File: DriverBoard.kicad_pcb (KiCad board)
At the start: 2 copper layers, 80 x 60 mm, 90 parts, among them J1 Conn_02x07_Odd_Even, J2 Conn_02x07_Odd_Even, Q1 HYG025N06LS1C2, Q2 HYG025N06LS1C2, Q3 HYG025N06LS1C2, Q4 HYG025N06LS1C2, Q5 HYG025N06LS1C2, Q6 HYG025N06LS1C2, U2 SCT2610, U4 SCT2420, U5 XT30PW-M

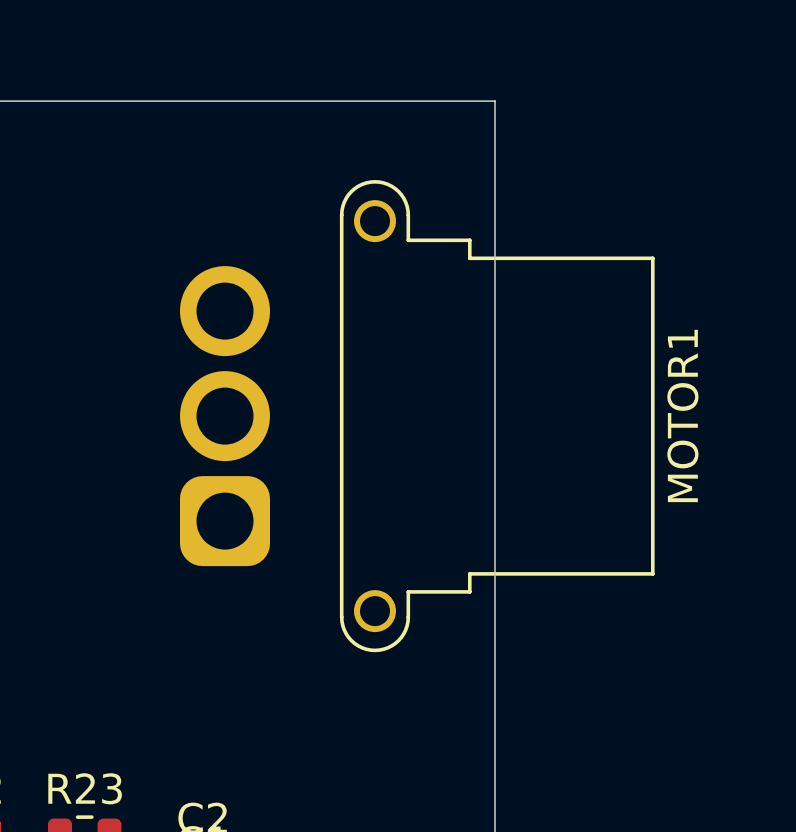
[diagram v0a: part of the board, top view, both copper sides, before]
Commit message: 工程增加环境变量
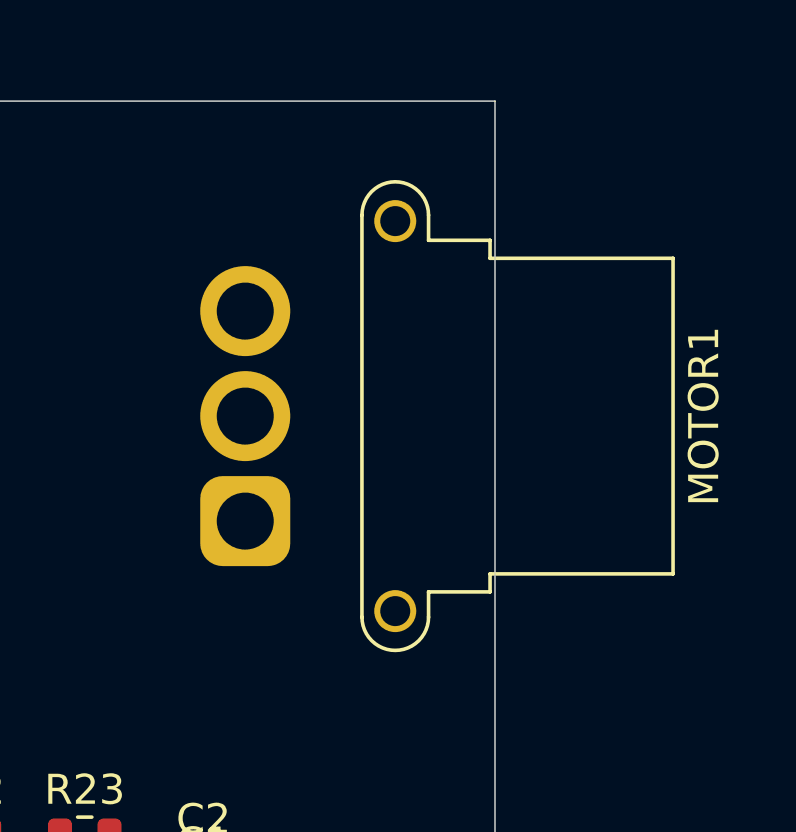
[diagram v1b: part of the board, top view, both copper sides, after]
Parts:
- moved MOTOR1 0.68 mm to (188.7, 63.0)

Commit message: 增加DXF文件夹
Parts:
- moved J1 42.0 mm to (122.0, 61.0)
- moved J2 36.1 mm to (123.5, 92.5)
- moved Q2 16.3 mm to (180.9, 63.9)
- moved Q1 15.4 mm to (172.9, 69.7)
- moved Q4 14.0 mm to (181.0, 57.9)
- moved Q6 13.5 mm to (180.5, 69.7)
- moved D1 11.2 mm to (153.0, 85.0), turned to 180 degrees
- moved Q5 8.53 mm to (173.7, 58.4)
- moved MOTOR1 4.55 mm to (188.0, 67.5)
- moved Q3 4.01 mm to (173.0, 64.2)
- moved U5 1.19 mm to (124.7, 81.5)
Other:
- outline, holes or cut-outs redrawn
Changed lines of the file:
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@@
 	(footprint "footprints:XT30PW-F_1x02_P2.50mm_Horizontal"
 		(layer "F.Cu")
-		(at 125.15 80.425 90)
+		(at 124.65 81.5 90)
 		(descr "Connector XT30 Horizontal PCB Female, https://www.tme.eu/Document/f383737e340bfdab1f665284174b4ea2/XT30PW-F.pdf")
 		(tags "RC Connector XT30")
@@
 	(footprint "Diode_SMD:D_SMB"
 		(layer "F.Cu")
-		(at 163.675 81.61)
+		(at 153 85 180)
 		(descr "Diode SMB (DO-214AA)")
 		(tags "Diode SMB (DO-214AA)")
@@
 		)
 		(property "Datasheet" ""
-			(at 0 0 0)
+			(at 0 0 180)
 			(unlocked yes)
 			(layer "F.Fab")
@@
 		)
 		(property "Description" ""
-			(at 0 0 0)
+			(at 0 0 180)
 			(unlocked yes)
 			(layer "F.Fab")
@@
 		(attr smd)
 		(fp_line
-			(start -3.66 -2.15)
-			(end -3.66 2.15)
+			(start -3.66 2.15)
+			(end 2.15 2.15)
 			(stroke
 				(width 0.12)
@@
 		)
 		(fp_line
-			(start -3.66 2.15)
-			(end 2.15 2.15)
+			(start -3.66 -2.15)
+			(end -3.66 2.15)
 			(stroke
 				(width 0.12)
@@
 		)
 		(fp_line
-			(start -3.65 -2.25)
-			(end 3.65 -2.25)
+			(start 3.65 2.25)
+			(end -3.65 2.25)
 			(stroke
 				(width 0.05)
@@
 		)
 		(fp_line
-			(start -3.65 2.25)
-			(end -3.65 -2.25)
+			(start 3.65 -2.25)
+			(end 3.65 2.25)
 			(stroke
 				(width 0.05)
@@
 		)
 		(fp_line
-			(start 3.65 -2.25)
-			(end 3.65 2.25)
+			(start -3.65 2.25)
+			(end -3.65 -2.25)
 			(stroke
 				(width 0.05)
@@
 		)
 		(fp_line
-			(start 3.65 2.25)
-			(end -3.65 2.25)
+			(start -3.65 -2.25)
+			(end 3.65 -2.25)
 			(stroke
 				(width 0.05)
@@
 		)
 		(fp_line
-			(start -2.3 2)
-			(end -2.3 -2)
+			(start 2.3 2)
+			(end -2.3 2)
 			(stroke
 				(width 0.1)
@@
 		)
 		(fp_line
-			(start -0.64944 -0.79908)
-			(end -0.64944 0.80112)
+			(start 2.3 -2)
+			(end 2.3 2)
 			(stroke
 				(width 0.1)
@@
 		)
 		(fp_line
-			(start -0.64944 0.00102)
-			(end -1.55114 0.00102)
+			(start 2.3 -2)
+			(end -2.3 -2)
 			(stroke
 				(width 0.1)
@@
 		)
 		(fp_line
-			(start -0.64944 0.00102)
+			(start 0.50118 0.75032)
 			(end 0.50118 -0.79908)
 			(stroke
@@
 		)
 		(fp_line
-			(start -0.64944 0.00102)
-			(end 0.50118 0.75032)
+			(start 0.50118 0.00102)
+			(end 1.4994 0.00102)
 			(stroke
 				(width 0.1)
@@
 		)
 		(fp_line
-			(start 0.50118 0.00102)
-			(end 1.4994 0.00102)
+			(start -0.64944 0.00102)
+			(end 0.50118 0.75032)
 			(stroke
 				(width 0.1)
@@
 		)
 		(fp_line
-			(start 0.50118 0.75032)
+			(start -0.64944 0.00102)
 			(end 0.50118 -0.79908)
 			(stroke
@@
 		)
 		(fp_line
-			(start 2.3 -2)
-			(end -2.3 -2)
+			(start -0.64944 0.00102)
+			(end -1.55114 0.00102)
 			(stroke
 				(width 0.1)
@@
 		)
 		(fp_line
-			(start 2.3 -2)
-			(end 2.3 2)
+			(start -0.64944 -0.79908)
+			(end -0.64944 0.80112)
 			(stroke
 				(width 0.1)
@@
 		)
 		(fp_line
-			(start 2.3 2)
-			(end -2.3 2)
+			(start -2.3 2)
+			(end -2.3 -2)
 			(stroke
 				(width 0.1)
@@
 		)
 		(pad "1" smd roundrect
-			(at -2.15 0)
+			(at -2.15 0 180)
 			(size 2.5 2.3)
 			(layers "F.Cu" "F.Mask" "F.Paste")
@@
 		)
 		(pad "2" smd roundrect
-			(at 2.15 0)
+			(at 2.15 0 180)
 			(size 2.5 2.3)
 			(layers "F.Cu" "F.Mask" "F.Paste")
@@
 	(footprint "footprints:HYG025N06LS1C2-PDFN-8-1EP_6x5mm_P1.27mm_EP3x3mm"
 		(layer "F.Cu")
-		(at 175.275 60.9)
+		(at 173.045 64.23)
 		(descr "W-PDFN, 8 Pin (https://media-www.micron.com/-/media/client/global/documents/products/data-sheet/nor-flash/serial-nor/mt25q/die-rev-a/mt25q_qljs_u_256_aba_0.pdf#page=22), generated with kicad-footprint-generator ipc_noLead_generator.py")
 		(tags "W-PDFN NoLead")
@@
 	(footprint "footprints:MR30PW-FB_1x03_P3.50mm_Horizontal"
 		(layer "F.Cu")
-		(at 188.675 63 -90)
+		(at 188 67.5 -90)
 		(descr "Connector MR30 Horizontal PCB Female, https://www.tme.eu/Document/4a6895c4a2c7eddf355b391fd904cb53/MR30PW-FB.pdf")
 		(tags "RC Connector MR30")
@@
 	(footprint "footprints:HYG025N06LS1C2-PDFN-8-1EP_6x5mm_P1.27mm_EP3x3mm"
 		(layer "F.Cu")
-		(at 167.35 66.75)
+		(at 180.51 69.71)
 		(descr "W-PDFN, 8 Pin (https://media-www.micron.com/-/media/client/global/documents/products/data-sheet/nor-flash/serial-nor/mt25q/die-rev-a/mt25q_qljs_u_256_aba_0.pdf#page=22), generated with kicad-footprint-generator ipc_noLead_generator.py")
 		(tags "W-PDFN NoLead")
@@
 	(footprint "footprints:HYG025N06LS1C2-PDFN-8-1EP_6x5mm_P1.27mm_EP3x3mm"
 		(layer "F.Cu")
-		(at 175.75 66.635)
+		(at 173.65 58.365)
 		(descr "W-PDFN, 8 Pin (https://media-www.micron.com/-/media/client/global/documents/products/data-sheet/nor-flash/serial-nor/mt25q/die-rev-a/mt25q_qljs_u_256_aba_0.pdf#page=22), generated with kicad-footprint-generator ipc_noLead_generator.py")
 		(tags "W-PDFN NoLead")
@@
 	(footprint "footprints:HYG025N06LS1C2-PDFN-8-1EP_6x5mm_P1.27mm_EP3x3mm"
 		(layer "F.Cu")
-		(at 167.925 53.98)
+		(at 180.91 63.865)
 		(descr "W-PDFN, 8 Pin (https://media-www.micron.com/-/media/client/global/documents/products/data-sheet/nor-flash/serial-nor/mt25q/die-rev-a/mt25q_qljs_u_256_aba_0.pdf#page=22), generated with kicad-footprint-generator ipc_noLead_generator.py")
 		(tags "W-PDFN NoLead")
@@
 	(footprint "footprints:HYG025N06LS1C2-PDFN-8-1EP_6x5mm_P1.27mm_EP3x3mm"
 		(layer "F.Cu")
-		(at 175.35 54.48)
+		(at 172.87 69.71)
 		(descr "W-PDFN, 8 Pin (https://media-www.micron.com/-/media/client/global/documents/products/data-sheet/nor-flash/serial-nor/mt25q/die-rev-a/mt25q_qljs_u_256_aba_0.pdf#page=22), generated with kicad-footprint-generator ipc_noLead_generator.py")
 		(tags "W-PDFN NoLead")
@@
 	(footprint "Connector_PinSocket_1.27mm:PinSocket_2x07_P1.27mm_Vertical_SMD"
 		(layer "F.Cu")
-		(at 121.8 103)
+		(at 122 61)
 		(descr "surface-mounted straight socket strip, 2x07, 1.27mm pitch, double cols (from Kicad 4.0.7!), script generated")
 		(tags "Surface mounted socket strip SMD 2x07 1.27mm double row")
@@
 	(footprint "footprints:HYG025N06LS1C2-PDFN-8-1EP_6x5mm_P1.27mm_EP3x3mm"
 		(layer "F.Cu")
-		(at 167.35 60.75)
+		(at 181.01 57.865)
 		(descr "W-PDFN, 8 Pin (https://media-www.micron.com/-/media/client/global/documents/products/data-sheet/nor-flash/serial-nor/mt25q/die-rev-a/mt25q_qljs_u_256_aba_0.pdf#page=22), generated with kicad-footprint-generator ipc_noLead_generator.py")
 		(tags "W-PDFN NoLead")
@@
 	(footprint "Connector_PinSocket_1.27mm:PinSocket_2x07_P1.27mm_Vertical_SMD"
 		(layer "F.Cu")
-		(at 121.8 56.46)
+		(at 123.5 92.5)
 		(descr "surface-mounted straight socket strip, 2x07, 1.27mm pitch, double cols (from Kicad 4.0.7!), script generated")
 		(tags "Surface mounted socket strip SMD 2x07 1.27mm double row")
@@
 		)
 	)
-	(gr_line
-		(start 117 78)
-		(end 197 78)
+	(gr_circle
+		(center 121 53.5)
+		(end 122.6 53.5)
+		(stroke
+			(width 0.5)
+			(type default)
+		)
+		(fill no)
+		(layer "Dwgs.User")
+	)
+	(gr_circle
+		(center 121 103.5)
+		(end 122.6 103.5)
+		(stroke
+			(width 0.5)
+			(type default)
+		)
+		(fill no)
+		(layer "Dwgs.User")
+	)
+	(gr_arc
+		(start 122 108.5)
+		(mid 117.757359 106.742641)
+		(end 116 102.5)
+		(stroke
+			(width 0.5)
+			(type solid)
+		)
+		(layer "Edge.Cuts")
+	)
+	(gr_arc
+		(start 190 48.5)
+		(mid 194.242641 50.257359)
+		(end 196 54.5)
 		(stroke
-			(width 0.1)
+			(width 0.5)
 			(type solid)
 		)
-		(layer "F.SilkS")
+		(layer "Edge.Cuts")
+	)
+	(gr_arc
+		(start 116 54.5)
+		(mid 117.757359 50.257359)
+		(end 122 48.5)
+		(stroke
+			(width 0.5)
+			(type solid)
+		)
+		(layer "Edge.Cuts")
 	)
 	(gr_line
-		(start 117 49)
-		(end 197 49)
+		(start 116 54.5)
+		(end 116 102.5)
 		(stroke
-			(width 0.05)
-			(type default)
+			(width 0.5)
+			(type solid)
+		)
+		(layer "Edge.Cuts")
+	)
+	(gr_circle
+		(center 191 103.5)
+		(end 192.6 103.5)
+		(stroke
+			(width 0.5)
+			(type solid)
 		)
+		(fill no)
 		(layer "Edge.Cuts")
 	)
 	(gr_line
-		(start 197 109)
-		(end 117 109)
+		(start 190 48.5)
+		(end 122 48.5)
 		(stroke
-			(width 0.05)
-			(type default)
+			(width 0.5)
+			(type solid)
+		)
+		(layer "Edge.Cuts")
+	)
+	(gr_arc
+		(start 196 102.5)
+		(mid 194.242641 106.742641)
+		(end 190 108.5)
+		(stroke
+			(width 0.5)
+			(type solid)
 		)
 		(layer "Edge.Cuts")
 	)
 	(gr_line
-		(start 197 49)
-		(end 197 109)
+		(start 196 102.5)
+		(end 196 54.5)
 		(stroke
-			(width 0.05)
-			(type default)
+			(width 0.5)
+			(type solid)
+		)
+		(layer "Edge.Cuts")
+	)
+	(gr_circle
+		(center 191 53.5)
+		(end 192.6 53.5)
+		(stroke
+			(width 0.5)
+			(type solid)
 		)
+		(fill no)
 		(layer "Edge.Cuts")
 	)
 	(gr_line
-		(start 117 109)
-		(end 117 49)
+		(start 122 108.5)
+		(end 190 108.5)
 		(stroke
-			(width 0.05)
-			(type default)
+			(width 0.5)
+			(type solid)
 		)
 		(layer "Edge.Cuts")
 	)
+	(gr_line
+		(start 116 78.5)
+		(end 196 78.5)
+		(stroke
+			(width 0.5)
+			(type solid)
+		)
+		(layer "User.1")
+	)
 	(embedded_fonts no)

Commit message: 三相桥基极增加回流路径,增加VDC的输入电容
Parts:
- removed U5: XT30PW-M, footprints:XT30PW-F_1x02_P2.50mm_Horizontal
- added C30: 4.7uF, Capacitor_SMD:C_1206_3216Metric, F.Cu at (176.5, 90.0)
- added C31: 4.7uF, Capacitor_SMD:C_1206_3216Metric, F.Cu at (176.5, 93.0)
- added C35: 4.7uF, Capacitor_SMD:C_1206_3216Metric, F.Cu at (176.5, 96.0)
- added C36: 4.7uF, Capacitor_SMD:C_1206_3216Metric, F.Cu at (176.5, 99.0)
- added C37: 4.7uF, Capacitor_SMD:C_1206_3216Metric, F.Cu at (176.5, 102.0)
- added C38: 4.7uF, Capacitor_SMD:C_1206_3216Metric, F.Cu at (176.5, 105.0)
- added D10: SODF107-SH, Diode_SMD:D_SOD-123F, F.Cu at (162.4, 103.0)
- added D4: SODF107-SH, Diode_SMD:D_SOD-123F, F.Cu at (162.3, 89.0)
- added D5: SODF107-SH, Diode_SMD:D_SOD-123F, F.Cu at (162.4, 91.3)
- added D6: SODF107-SH, Diode_SMD:D_SOD-123F, F.Cu at (162.4, 94.0)
- added D8: SODF107-SH, Diode_SMD:D_SOD-123F, F.Cu at (162.4, 97.0)
- added D9: SODF107-SH, Diode_SMD:D_SOD-123F, F.Cu at (162.4, 100.0)
- added U6: ~, footprints:XT30PW-F_1x02_P2.50mm_Horizontal, F.Cu at (122.0, 80.0)
- D2, D3, D7: value SS1P3L-M3 -> SODF107-SH; footprint Diode_SMD:D_SMP_DO-220AA -> Diode_SMD:D_SOD-123F
- moved D2 47.0 mm to (167.3, 90.0)
- moved D3 46.3 mm to (167.3, 93.3)
- moved D7 45.6 mm to (167.3, 96.7)

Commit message: 优化原理图
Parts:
- added C27: 0.1uF/100V, Capacitor_SMD:C_0603_1608Metric, F.Cu at (169.0, 78.5)
- added C8: 2.2uF, Capacitor_SMD:C_0603_1608Metric, F.Cu at (133.2, 74.0)
- moved C28 44.2 mm to (181.4, 52.0), turned to 90 degrees
- moved C25 41.0 mm to (179.2, 52.0), turned to 90 degrees
- moved C23 38.0 mm to (177.0, 52.0), turned to 90 degrees
- moved R28 26.8 mm to (161.2, 65.3), turned to 90 degrees
- moved R22 26.2 mm to (136.5, 61.0)
- moved R29 25.1 mm to (159.6, 65.3), turned to 90 degrees
- moved R18 22.6 mm to (129.3, 66.0)
- moved C20 22.6 mm to (134.0, 63.4)
- moved C21 22.6 mm to (134.0, 65.9)
- moved R16 22.6 mm to (129.3, 63.5)
- moved R19 22.6 mm to (129.3, 68.5)
- moved R21 19.3 mm to (131.5, 51.0)
- moved R30 17.9 mm to (155.0, 68.4)
- moved R37 17.4 mm to (161.5, 61.8), turned to 90 degrees
- moved R35 17.0 mm to (158.0, 61.8), turned to 90 degrees
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- renumbered C10 to C1, C4 to C10, C13 to C11, C5 to C12, C15 to C13, C16 to C14, C17 to C15, C8 to C16, C6 to C17, C7 to C18, C26 to C19, C11 to C2, C27 to C20, C28 to C21, C29 to C22, C30 to C23, C36 to C24, C31 to C25, C37 to C26, C35 to C28, C38 to C29, C12 to C3, C20 to C30, C23 to C31, C9 to C32, C19 to C33, C33 to C34, C32 to C35, C34 to C36, C21 to C37, C22 to C38, C24 to C39, C18 to C4, C25 to C40, C1 to C5, C2 to C6, C3 to C7, C14 to C9, D3 to D10, D4 to D2, D5 to D3, D6 to D4, D8 to D5, D10 to D6, D9 to D7, D7 to D8, D2 to D9, L2 to L1, L1 to L2, Q6 to Q1, Q1 to Q2, Q2 to Q3, Q3 to Q4, Q4 to Q5, Q5 to Q6, R18 to R1, R22 to R10, R12 to R11, R13 to R12, R1 to R13, R2 to R14, R24 to R15, R25 to R16, R15 to R17, R26 to R18, R27 to R19, R19 to R2, R3 to R20, R28 to R21, R29 to R22, R4 to R23, R40 to R24, R43 to R25, R38 to R26, R39 to R27, R41 to R28, R42 to R29, R20 to R3, R44 to R30, R30 to R31, R31 to R32, R32 to R33, R33 to R34, R34 to R35, R35 to R36, R36 to R37, R37 to R38, R9 to R4, R10 to R5, R11 to R6, R23 to R7, R14 to R8, R21 to R9, U6 to U1, U4 to U2, U2 to U3, U1 to U4, U3 to U5
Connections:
- C23 pad 2: GND -> GNDPWR
- C24 pad 2: GND -> GNDPWR
- C25 pad 2: GND -> GNDPWR
- C26 pad 2: GND -> GNDPWR
- C28 pad 2: GND -> GNDPWR
- C29 pad 2: GND -> GNDPWR
- R17 pad 2: GND -> GNDPWR
- R20 pad 2: GND -> GNDPWR
- R23 pad 2: GND -> GNDPWR

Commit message: 修改板框文件
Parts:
- moved U1 60.1 mm to (182.4, 73.7), turned to -90 degrees
- moved D8 59.1 mm to (128.2, 52.4), turned to 180 degrees
- moved D10 53.2 mm to (128.2, 57.3), turned to 180 degrees
- moved D9 52.6 mm to (128.2, 54.8), turned to 180 degrees
- moved R7 52.3 mm to (131.1, 72.9)
- moved C4 51.5 mm to (123.9, 78.4)
- moved C15 48.6 mm to (127.2, 79.9)
- moved R16 46.9 mm to (175.4, 72.3)
- moved L1 46.5 mm to (140.2, 73.7), turned to 180 degrees
- moved C16 45.2 mm to (173.0, 82.5)
- moved R18 42.7 mm to (172.1, 65.6), turned to -90 degrees
- moved R15 40.5 mm to (180.0, 65.6), turned to 90 degrees
- moved C8 40.1 mm to (172.7, 81.0)
- moved D6 39.5 mm to (164.3, 61.6), turned to 90 degrees
- moved C20 39.0 mm to (172.5, 57.2), turned to -90 degrees
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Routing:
- net /Pre_Driver/W1: track 0.00 -> 33.8 mm, vias 0 -> 1
- net /Pre_Driver/V1: track 0.00 -> 23.0 mm, vias 0 -> 1
- net /Pre_Driver/U1: track 0.00 -> 10.8 mm, vias 0 -> 1
- net /ThreePhase/U1_CURR: track 0.00 -> 4.98 mm
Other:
- outline, holes or cut-outs redrawn

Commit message: 优化电源布局,优化中
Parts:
- moved R12 37.8 mm to (143.6, 93.7)
- moved R11 34.6 mm to (141.9, 93.7)
- moved R17 31.3 mm to (179.0, 36.6)
- moved R20 31.3 mm to (171.0, 36.6)
- moved R22 31.3 mm to (161.9, 41.0)
- moved R23 31.3 mm to (162.9, 36.6)
- moved C21 31.3 mm to (166.7, 26.0)
- moved C22 31.3 mm to (158.2, 26.0)
- moved D4 31.3 mm to (175.1, 30.3)
- moved Q3 31.3 mm to (171.0, 23.5)
- moved Q5 31.3 mm to (162.9, 23.5)
- moved D5 31.3 mm to (170.8, 39.1)
- moved Q4 31.3 mm to (171.0, 31.5)
- moved Q6 31.3 mm to (162.9, 31.5)
- moved R16 31.3 mm to (178.0, 41.0)
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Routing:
- net /Pre_Driver/W1: track 33.8 -> 0.00 mm
- net Net-(U3-FB): track 0.00 -> 27.4 mm, vias 0 -> 2
- net /Pre_Driver/V1: track 23.0 -> 0.00 mm, vias 1 -> 0
- net /Pre_Driver/U1: track 10.8 -> 0.00 mm
- net Net-(U3-COMP): track 0.00 -> 7.75 mm, vias 0 -> 2
- added copper zone on F.Cu, net Net-(D1-K)

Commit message: 布局初步结束
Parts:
- added MOTOR1: Conn_01x03, footprints:MR30PW-FB_1x03_P3.50mm_Horizontal, F.Cu at (182.3, 98.6)
- moved C4 32.6 mm to (156.1, 73.0), turned to 90 degrees
- moved C16 30.1 mm to (165.8, 71.8), turned to 180 degrees
- moved R12 28.7 mm to (163.1, 72.6), turned to -90 degrees
- moved R11 28.6 mm to (161.2, 72.6)
- moved C21 27.8 mm to (162.4, 53.4)
- moved C22 27.8 mm to (153.9, 53.4)
- moved D4 27.8 mm to (170.8, 57.8)
- moved D3 27.8 mm to (174.5, 66.5)
- moved R16 27.8 mm to (173.8, 68.5)
- moved R19 27.8 mm to (165.8, 68.7)
- moved R22 27.8 mm to (157.7, 68.4)
- moved R23 27.8 mm to (158.6, 64.1)
- moved C20 27.8 mm to (170.8, 53.4)
- moved D2 27.8 mm to (178.8, 57.8)
- moved D6 27.8 mm to (162.7, 57.8)
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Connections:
- U3 pad 11: unconnected-(U3-EP-Pad11) -> GND
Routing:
- net Net-(U3-FB): track 27.4 -> 0.00 mm, vias 2 -> 0
- net Net-(U2-FB): track 0.00 -> 10.2 mm
- net Net-(U3-COMP): track 7.75 -> 0.00 mm, vias 2 -> 0
- net Net-(U2-COMP): track 0.00 -> 2.84 mm
- net GND: track 0.00 -> 2.15 mm
- net Net-(C11-Pad1): track 0.00 -> 1.47 mm
- removed copper zone on F.Cu, net Net-(D1-K)
